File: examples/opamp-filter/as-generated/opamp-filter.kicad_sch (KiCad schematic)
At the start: 19 parts, among them J1 IN, J2 5V, J3 OUT, U1 MCP6001R, U2 MCP6001R

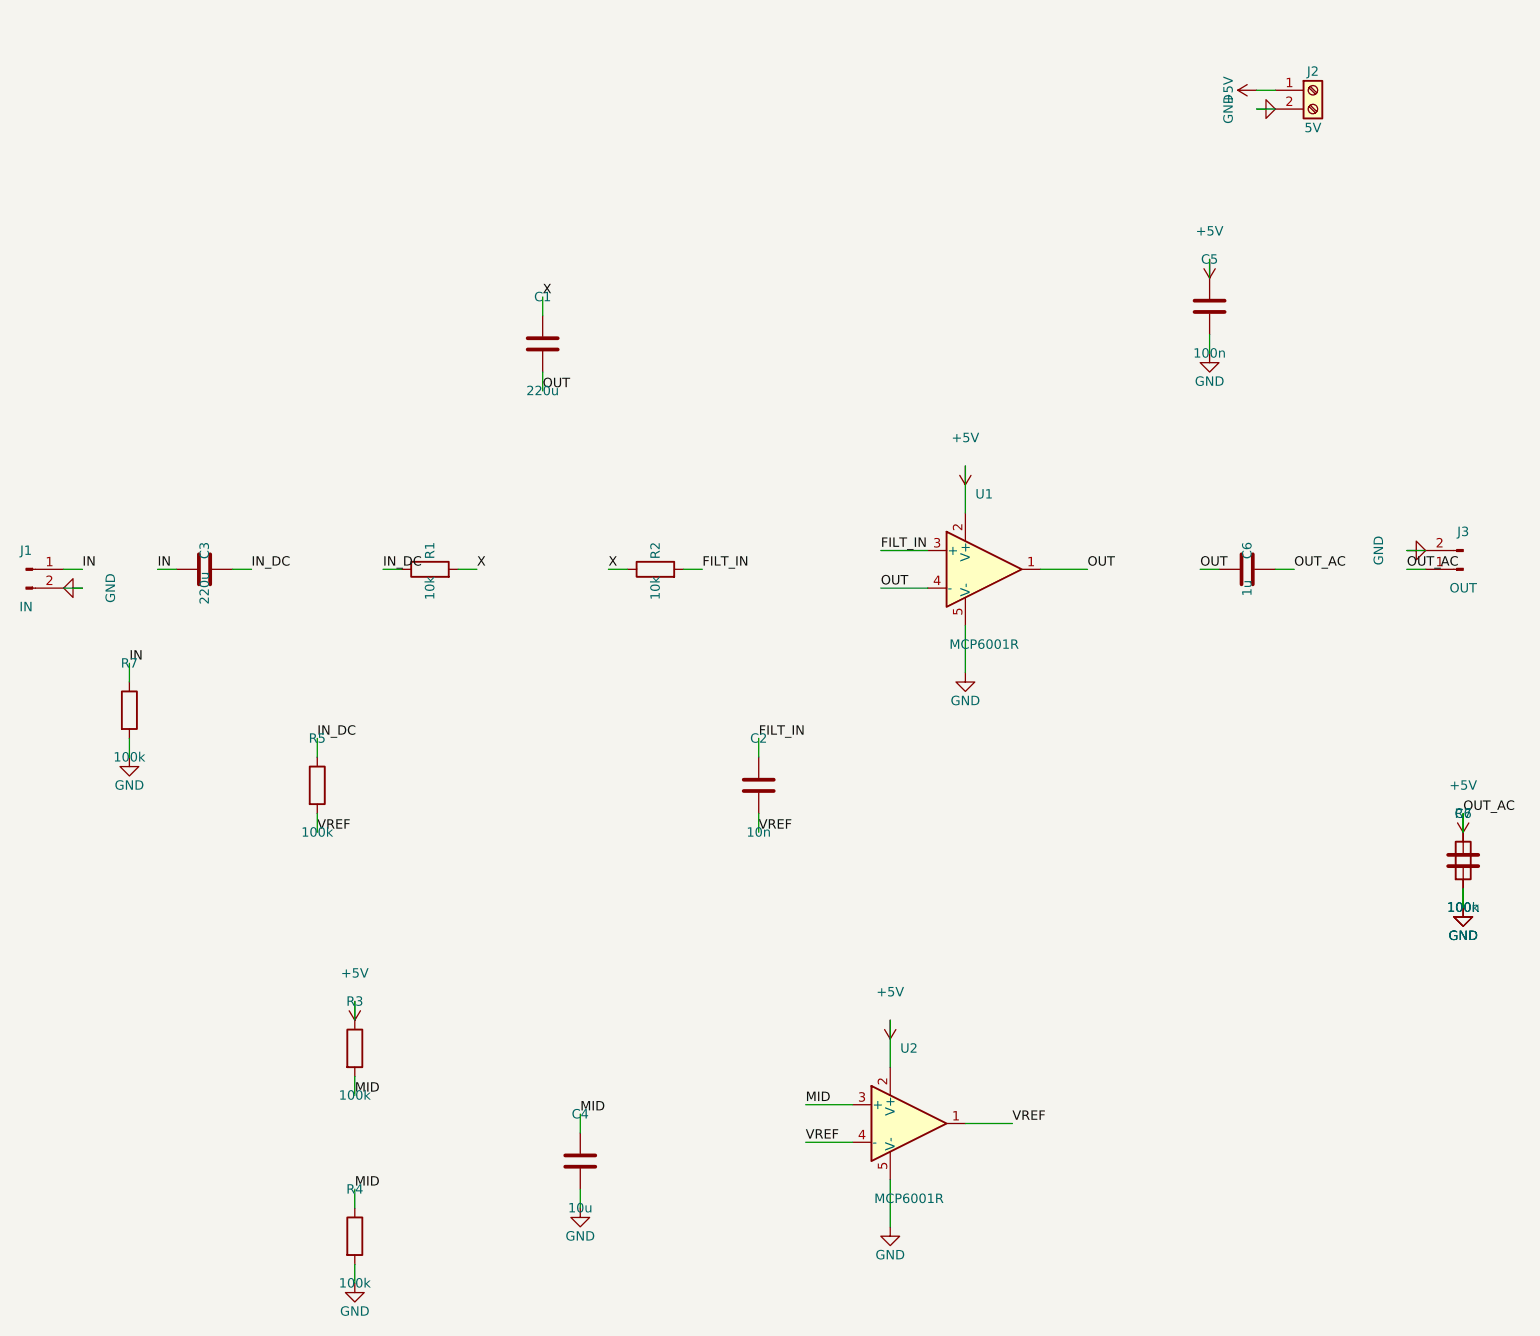
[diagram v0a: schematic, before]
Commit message: Regenerate the five with stitched pours, silk that speaks, and wires that never double back
All ten variants rebuilt by the fixed generator: reviewed boards carry
ground on both faces with the stitching ring (buck 35 vias, fpga 116),
thru_hole_only front pours, the board id and connector pin names in
silk, and the buck's explicit ground return; the sheets hook power up
through upright symbols and source-anchored flags with no overlapping
wires and no junction-less tees left. Every reviewed variant passes its
own gate with zero errors; every as-generated variant still fails, now
also for the rules this round added.

Co-Authored-By: Claude Fable 5 <noreply@anthropic.com>
Claude-Session: https://claude.ai/code/session_01DUj7Ltu92tWg159mCSacwY
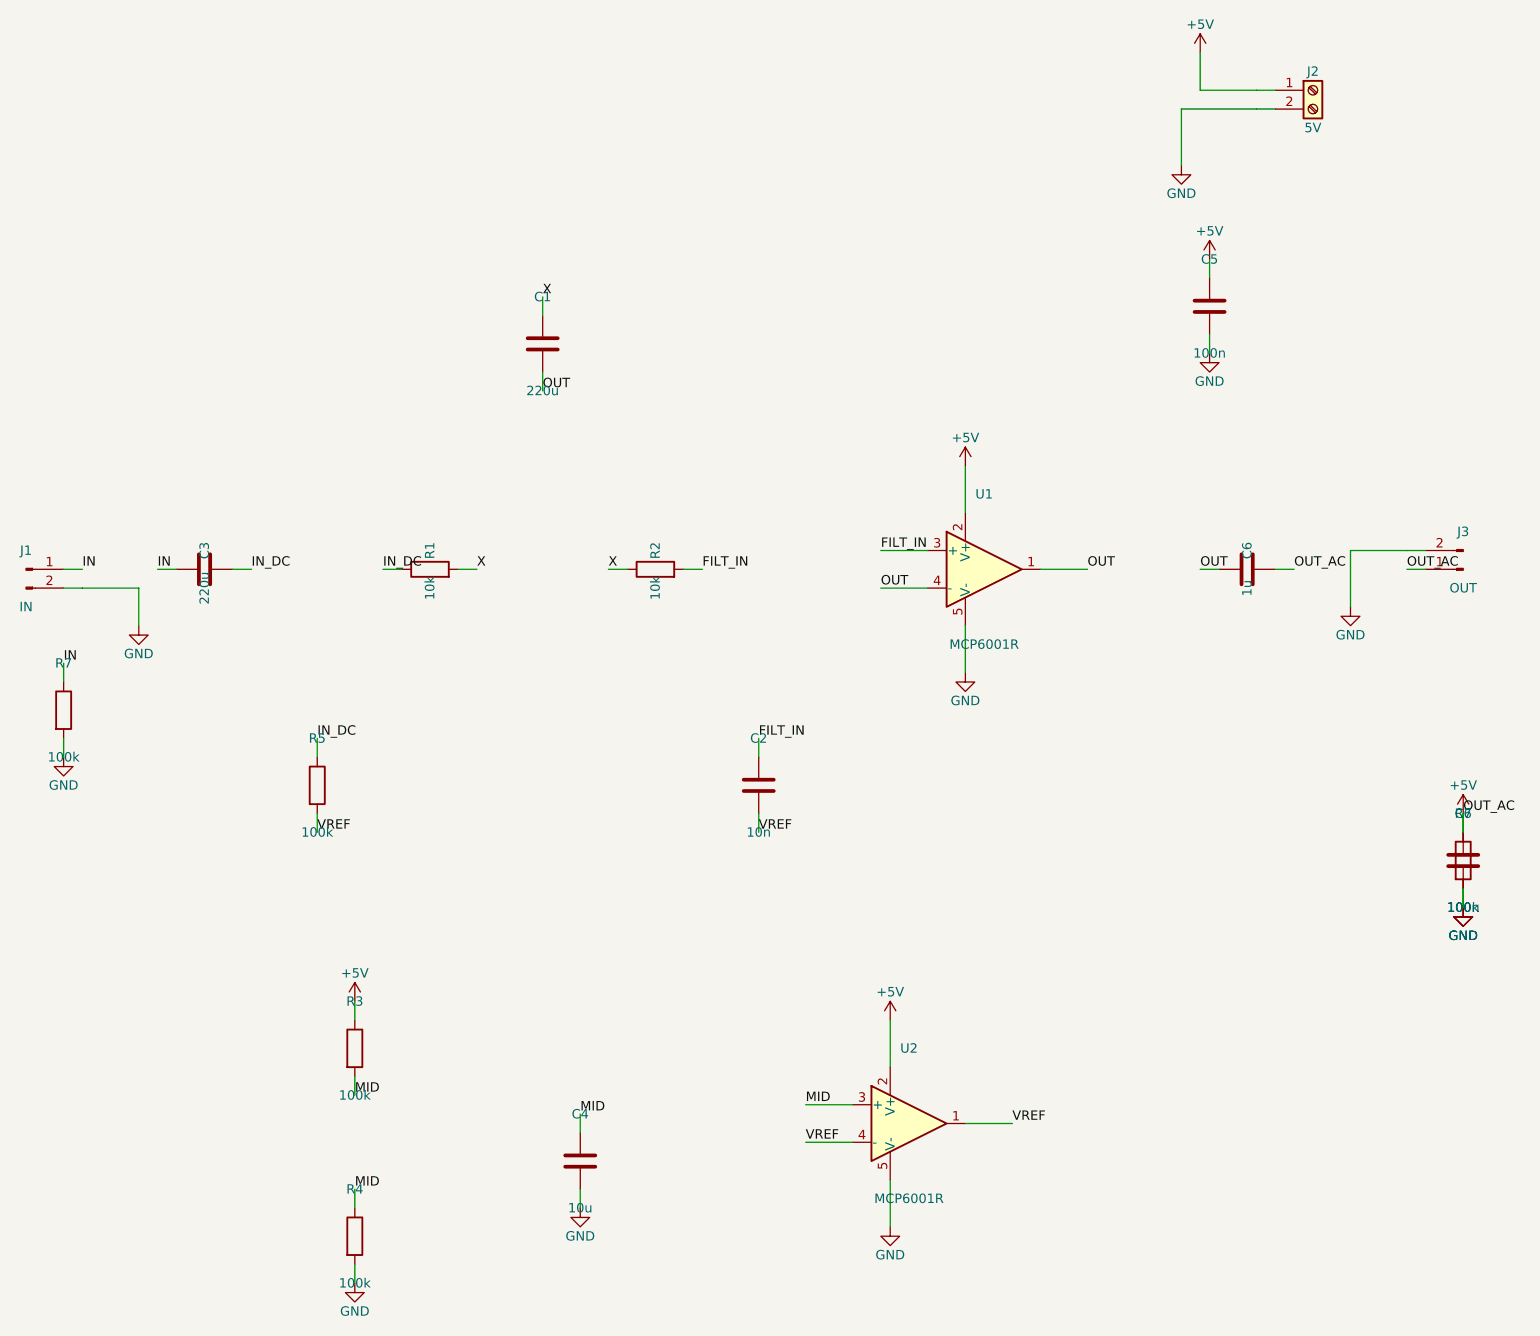
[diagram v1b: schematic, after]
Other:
- moved on the sheet: R7
